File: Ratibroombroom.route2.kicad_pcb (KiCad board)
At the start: 2 copper layers, 46 x 60 mm, 112 parts, among them J1 Conn_01x02_Male, J10 Conn_01x04_Male, J11 Conn_01x04_Male, J2 Conn_01x02_Male, J3 Conn_01x10_Male, J5 Conn_01x02_Male, J6 Conn_01x02_Male, J8 Conn_01x04_Male, J9 Conn_01x04_Male, Q1 IRLML6344, Q10 S8050, Q11 IRF7416PbF, Q2 IRLML6344, Q3 IRLML6344, Q4 IRLML6344, Q5 PT12-21B/TR8, Q6 PT12-21B/TR8, Q7 PT12-21B/TR8, Q8 PT12-21B/TR8, Q9 IRLML6344, SW1 B3U, SW2 B3U, SW3 PCM12, U1 AZ1117-3.3, U2 DRV8835, U3 AS5145B-HSST, U4 MPU-9250, U5 STM32F405RGTx, U6 AS5145B-HSST, U7 DRV8835, U8 L6932D1.2TR, U9 L6932D1.2TR, Y1 8MHZ

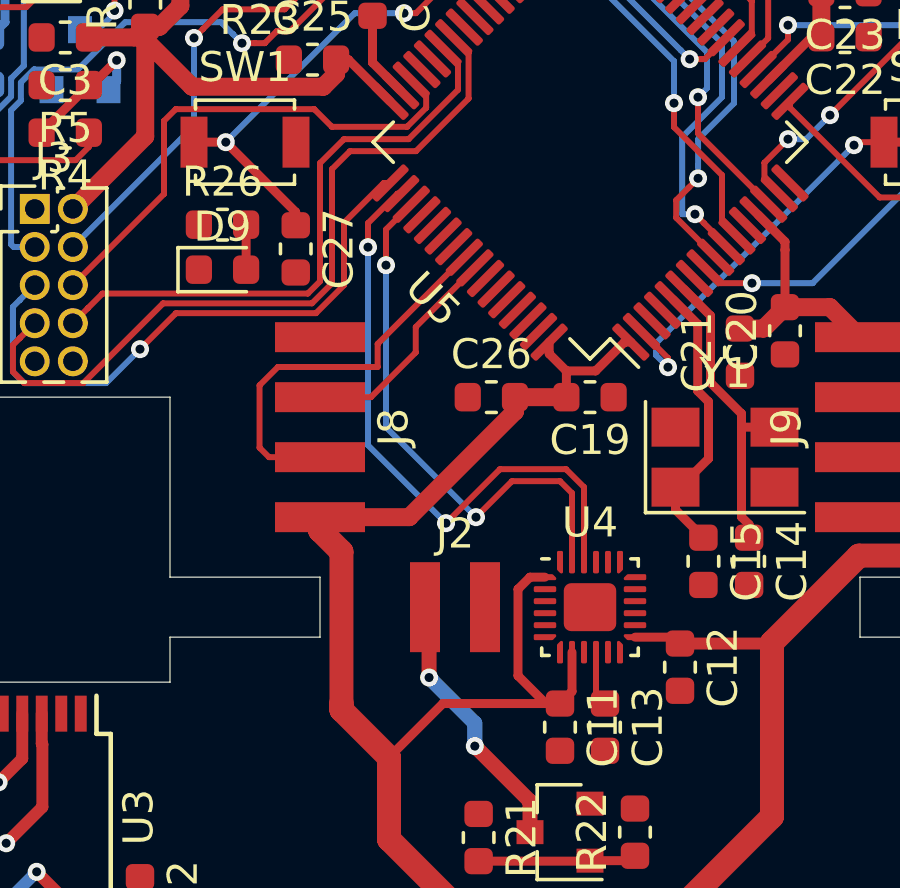
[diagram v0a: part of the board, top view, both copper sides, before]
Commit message: Partial PCB routing
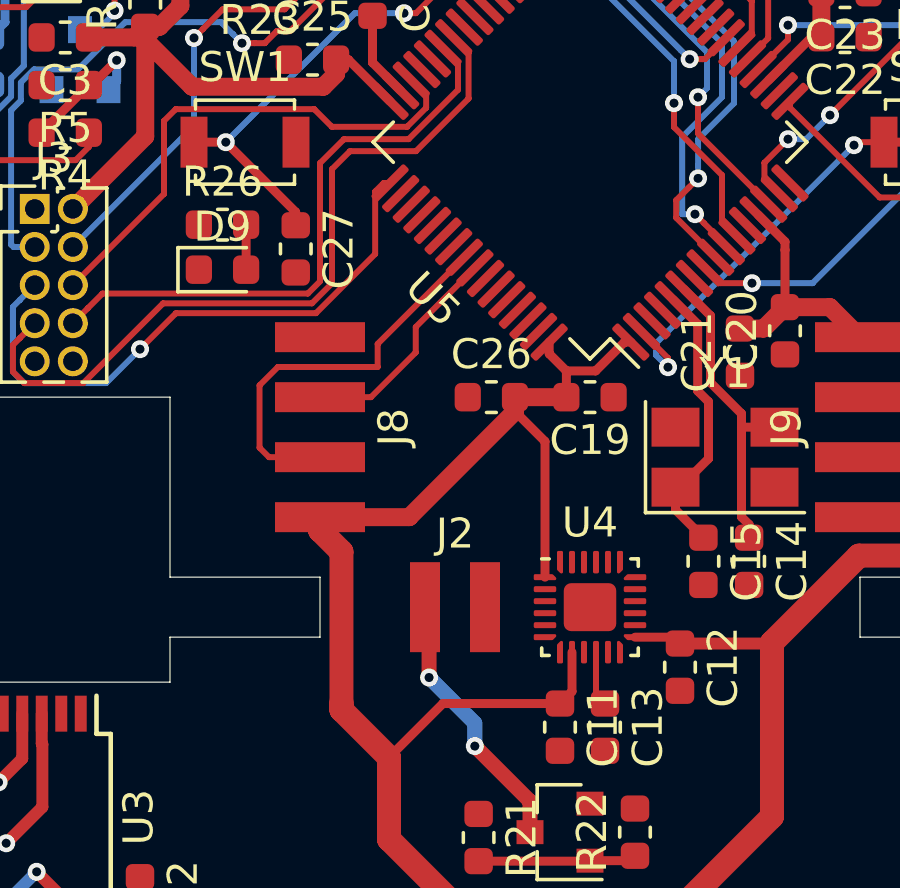
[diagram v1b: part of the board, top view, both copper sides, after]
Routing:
- net /IMU_CS: track 20.7 -> 0.00 mm, vias 2 -> 0
- net /IMU_SCK: track 18.2 -> 0.00 mm, vias 2 -> 0
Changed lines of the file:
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@@
     (thickness 1.6)
     (drawings 143)
-    (tracks 841)
+    (tracks 817)
     (zones 0)
     (modules 112)
@@
   (segment (start 140.0965 94.2125) (end 138.3 96.009) (width 0.3) (layer F.Cu) (net 2))
   (segment (start 144 94.2125) (end 140.0965 94.2125) (width 0.3) (layer F.Cu) (net 2))
+  (segment (start 143.5 85.475) (end 142.5 84.475) (width 0.3) (layer F.Cu) (net 2))
+  (segment (start 143.5 90) (end 143.5 85.475) (width 0.3) (layer F.Cu) (net 2))
   (segment (start 161.925 94.5) (end 161.975 94.55) (width 0.4) (layer F.Cu) (net 2))
   (segment (start 160 94.5) (end 161.925 94.5) (width 0.4) (layer F.Cu) (net 2))
@@
   (segment (start 136.5 65.5) (end 136.5 65.025) (width 0.6) (layer F.Cu) (net 2))
   (segment (start 136.5 65.025) (end 136.07299 64.59799) (width 0.6) (layer F.Cu) (net 2))
-  (segment (start 143.5 90) (end 143 90) (width 0.3) (layer F.Cu) (net 2))
-  (segment (start 143 90) (end 142.6 90.4) (width 0.3) (layer F.Cu) (net 2))
-  (segment (start 143.525 94.2125) (end 144 94.2125) (width 0.3) (layer F.Cu) (net 2))
-  (segment (start 142.6 93.2875) (end 143.525 94.2125) (width 0.3) (layer F.Cu) (net 2))
-  (segment (start 142.6 90.4) (end 142.6 93.2875) (width 0.3) (layer F.Cu) (net 2))
   (segment (start 155.905 113.3) (end 154.635 113.3) (width 0.8) (layer F.Cu) (net 4))
   (segment (start 157.5 112.78) (end 157.5 111) (width 0.8) (layer F.Cu) (net 4))
@@
   (segment (start 130.8 77.226) (end 127.762 80.264) (width 0.2) (layer F.Cu) (net 31))
   (segment (start 130.8 74.791398) (end 130.8 77.226) (width 0.2) (layer F.Cu) (net 31))
+  (segment (start 137.839054 79.227774) (end 135.866828 81.2) (width 0.2) (layer F.Cu) (net 32))
+  (segment (start 137.839054 77.145514) (end 137.839054 79.227774) (width 0.2) (layer F.Cu) (net 32))
+  (segment (start 138.335519 76.861181) (end 138.123387 76.861181) (width 0.2) (layer F.Cu) (net 32))
+  (segment (start 138.123387 76.861181) (end 137.839054 77.145514) (width 0.2) (layer F.Cu) (net 32))
   (via (at 130 82.4) (size 0.6) (drill 0.3) (layers F.Cu B.Cu) (net 32))
+  (segment (start 135.866828 81.2) (end 131.2 81.2) (width 0.2) (layer F.Cu) (net 32))
+  (segment (start 131.2 81.2) (end 130 82.4) (width 0.2) (layer F.Cu) (net 32))
   (segment (start 125.992001 80.763999) (end 126.492 80.264) (width 0.2) (layer B.Cu) (net 32))
   (segment (start 125.764999 80.991001) (end 125.992001 80.763999) (width 0.2) (layer B.Cu) (net 32))
@@
   (segment (start 126.143039 83.531001) (end 125.764999 83.152961) (width 0.2) (layer B.Cu) (net 32))
   (segment (start 130 82.4) (end 128.868999 83.531001) (width 0.2) (layer B.Cu) (net 32))
-  (segment (start 138.123387 76.861181) (end 136.8 78.184568) (width 0.2) (layer F.Cu) (net 32))
-  (segment (start 138.335519 76.861181) (end 138.123387 76.861181) (width 0.2) (layer F.Cu) (net 32))
-  (segment (start 131.2 81.2) (end 130 82.4) (width 0.2) (layer F.Cu) (net 32))
-  (segment (start 136.8 78.184568) (end 136.8 80.266828) (width 0.2) (layer F.Cu) (net 32))
-  (segment (start 135.866828 81.2) (end 131.2 81.2) (width 0.2) (layer F.Cu) (net 32))
-  (segment (start 136.8 80.266828) (end 135.866828 81.2) (width 0.2) (layer F.Cu) (net 32))
   (segment (start 140.103286 72.371052) (end 140.59975 72.867516) (width 0.2) (layer F.Cu) (net 33))
   (segment (start 128.261999 81.034001) (end 127.762 81.534) (width 0.2) (layer F.Cu) (net 33))
@@
   (segment (start 142.79197 109.75) (end 142.839959 109.797989) (width 0.3) (layer F.Cu) (net 76))
   (segment (start 141.95 109.75) (end 142.79197 109.75) (width 0.3) (layer F.Cu) (net 76))
-  (via (at 138.2 79.6) (size 0.6) (drill 0.3) (layers F.Cu B.Cu) (net 85))
-  (segment (start 138.2 78.410912) (end 138.2 79.6) (width 0.2) (layer F.Cu) (net 85))
-  (segment (start 139.042625 77.568287) (end 138.2 78.410912) (width 0.2) (layer F.Cu) (net 85))
-  (via (at 141.2 88) (size 0.6) (drill 0.3) (layers F.Cu B.Cu) (net 85))
-  (segment (start 141.2 88) (end 142.4 86.8) (width 0.2) (layer F.Cu) (net 85))
-  (segment (start 142.4 86.8) (end 144 86.8) (width 0.2) (layer F.Cu) (net 85))
-  (segment (start 144.4 87.2) (end 144.4 89.5) (width 0.2) (layer F.Cu) (net 85))
-  (segment (start 144 86.8) (end 144.4 87.2) (width 0.2) (layer F.Cu) (net 85))
-  (segment (start 138.2 79.6) (end 138.2 85) (width 0.2) (layer B.Cu) (net 85))
-  (segment (start 138.2 85) (end 141.2 88) (width 0.2) (layer B.Cu) (net 85))
-  (segment (start 138.689072 77.214734) (end 138.585266 77.214734) (width 0.2) (layer F.Cu) (net 86))
-  (via (at 137.6 79) (size 0.6) (drill 0.3) (layers F.Cu B.Cu) (net 86))
-  (segment (start 138.585266 77.214734) (end 137.6 78.2) (width 0.2) (layer F.Cu) (net 86))
-  (segment (start 137.6 78.2) (end 137.6 79) (width 0.2) (layer F.Cu) (net 86))
-  (via (at 140.2 88.2) (size 0.6) (drill 0.3) (layers F.Cu B.Cu) (net 86))
-  (segment (start 140.2 88.2) (end 142 86.4) (width 0.2) (layer F.Cu) (net 86))
-  (segment (start 142 86.4) (end 144.2 86.4) (width 0.2) (layer F.Cu) (net 86))
-  (segment (start 144.2 86.4) (end 144.8 87) (width 0.2) (layer F.Cu) (net 86))
-  (segment (start 144.8 87) (end 144.8 89.5) (width 0.2) (layer F.Cu) (net 86))
-  (segment (start 137.6 85.6) (end 140.2 88.2) (width 0.2) (layer B.Cu) (net 86))
-  (segment (start 137.6 79) (end 137.6 85.6) (width 0.2) (layer B.Cu) (net 86))
   (segment (start 148.05 109.25) (end 146.133984 109.25) (width 0.3) (layer F.Cu) (net 97))
   (segment (start 146.133984 109.25) (end 145.949992 109.066008) (width 0.3) (layer F.Cu) (net 97))
